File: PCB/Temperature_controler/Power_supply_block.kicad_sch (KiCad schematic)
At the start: 30 parts, among them J10 24V IN, U4 MP1584EN-LF-Z, U5 MP1584EN-LF-Z

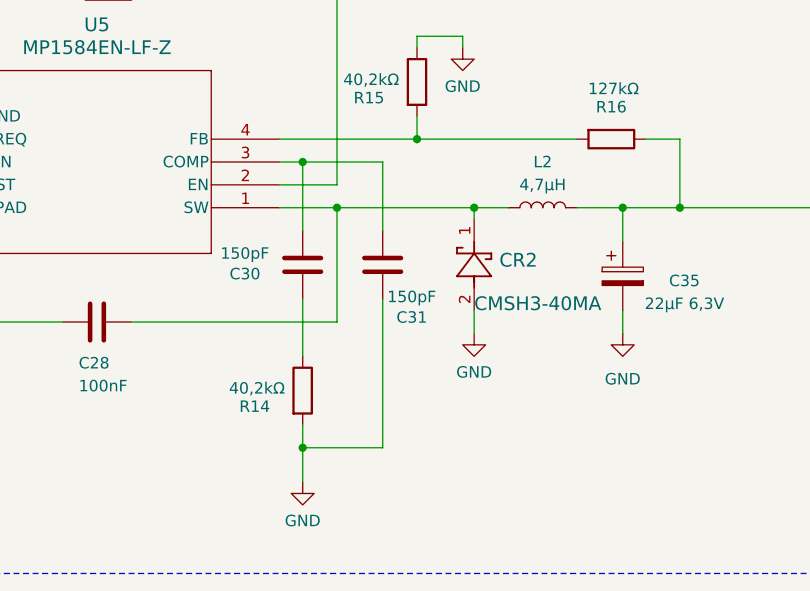
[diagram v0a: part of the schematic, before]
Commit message: PCB traces changed
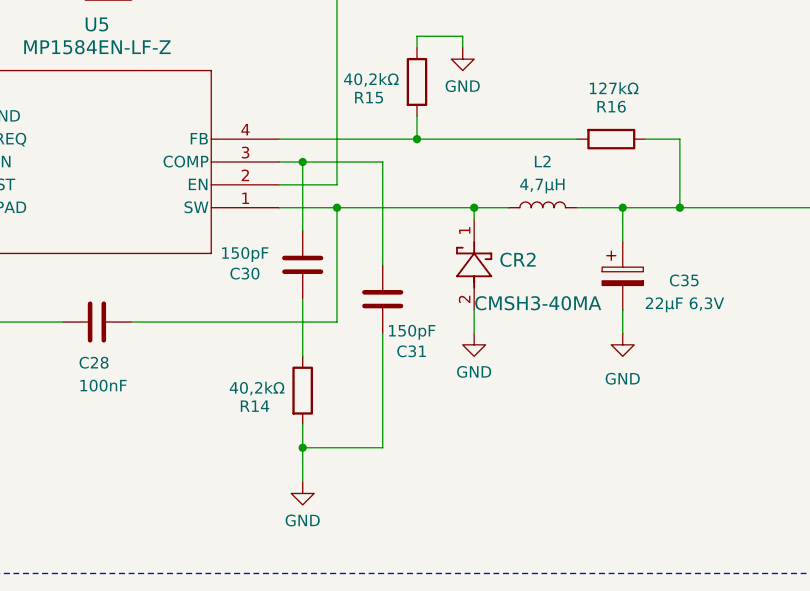
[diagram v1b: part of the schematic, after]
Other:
- moved on the sheet: C31
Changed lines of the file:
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@@
 	(wire
 		(pts
-			(xy 138.43 194.31) (xy 138.43 186.69)
+			(xy 138.43 198.12) (xy 138.43 186.69)
 		)
 		(stroke
@@
 	(wire
 		(pts
-			(xy 138.43 201.93) (xy 138.43 218.44)
+			(xy 138.43 205.74) (xy 138.43 218.44)
 		)
 		(stroke
@@
 	(symbol
 		(lib_id "Device:C")
-		(at 138.43 198.12 0)
+		(at 138.43 201.93 0)
 		(unit 1)
 		(exclude_from_sim no)
@@
 		(dnp no)
 		(property "Reference" "C31"
-			(at 139.954 203.962 0)
+			(at 139.954 207.772 0)
 			(effects
 				(font
@@
 		)
 		(property "Value" "150pF"
-			(at 138.938 201.676 0)
+			(at 138.938 205.486 0)
 			(effects
 				(font
@@
 		)
 		(property "Footprint" "Capacitor_SMD:C_0805_2012Metric_Pad1.18x1.45mm_HandSolder"
-			(at 139.3952 201.93 0)
+			(at 139.3952 205.74 0)
 			(effects
 				(font
@@
 		)
 		(property "Datasheet" "~"
-			(at 138.43 198.12 0)
+			(at 138.43 201.93 0)
 			(effects
 				(font
@@
 		)
 		(property "Description" "Unpolarized capacitor"
-			(at 138.43 198.12 0)
+			(at 138.43 201.93 0)
 			(effects
 				(font
